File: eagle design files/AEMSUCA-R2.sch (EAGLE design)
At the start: 16 parts, among them IC1 AEM10941, Q1 DMG1012UW

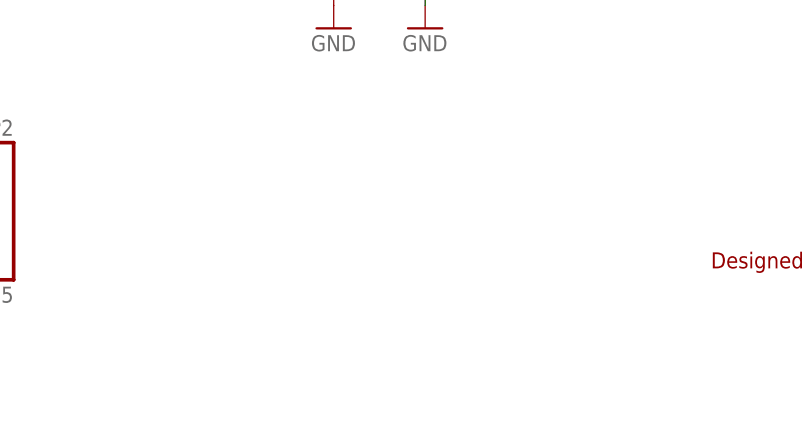
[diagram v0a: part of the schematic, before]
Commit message: updated PCB and gerbers to reduce solderpaste under IC1 to 50%
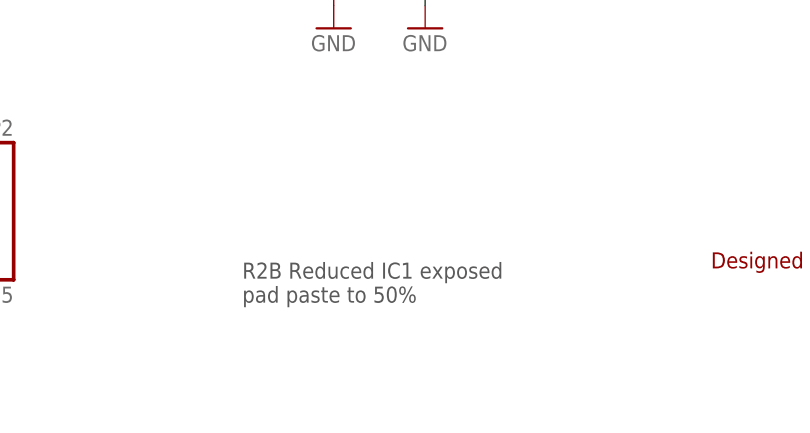
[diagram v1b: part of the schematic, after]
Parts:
- IC1: device sodaq:AEM10941 -> TSEM:AEM10941
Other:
- note added: "R2B Reduced IC1 exposed pad paste to 50%"
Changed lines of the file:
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@@
 </classes>
 <parts>
-<part name="IC1" library="sodaq" deviceset="AEM10941" device="" package3d_urn="urn:adsk.eagle:package:2265650/1" value="AEM10941"/>
+<part name="IC1" library="TSEM" deviceset="AEM10941" device="" value="AEM10941"/>
 <part name="GND6" library="supply1" deviceset="GND" device=""/>
 <part name="L2" library="TSEM" deviceset="L" device="0603_10UH" value="10uH"/>
@@
 <text x="15.24" y="55.88" size="1.778" layer="97">selects MPP voltage ratio,
 see datasheet AEM109410</text>
+<text x="163.83" y="16.51" size="1.778" layer="97">R2B Reduced IC1 exposed
+pad paste to 50%</text>
 </plain>
 <instances>
@@
 will not be understood (or retained) with this version.
 </note>
-<note version="8.3" severity="warning">
-Since Version 8.3, EAGLE supports the association of 3D packages
-with devices in libraries, schematics, and board files. Those 3D
-packages will not be understood (or retained) with this version.
-</note>
 </compatibility>
